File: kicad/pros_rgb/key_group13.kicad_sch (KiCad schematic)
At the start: 16 parts

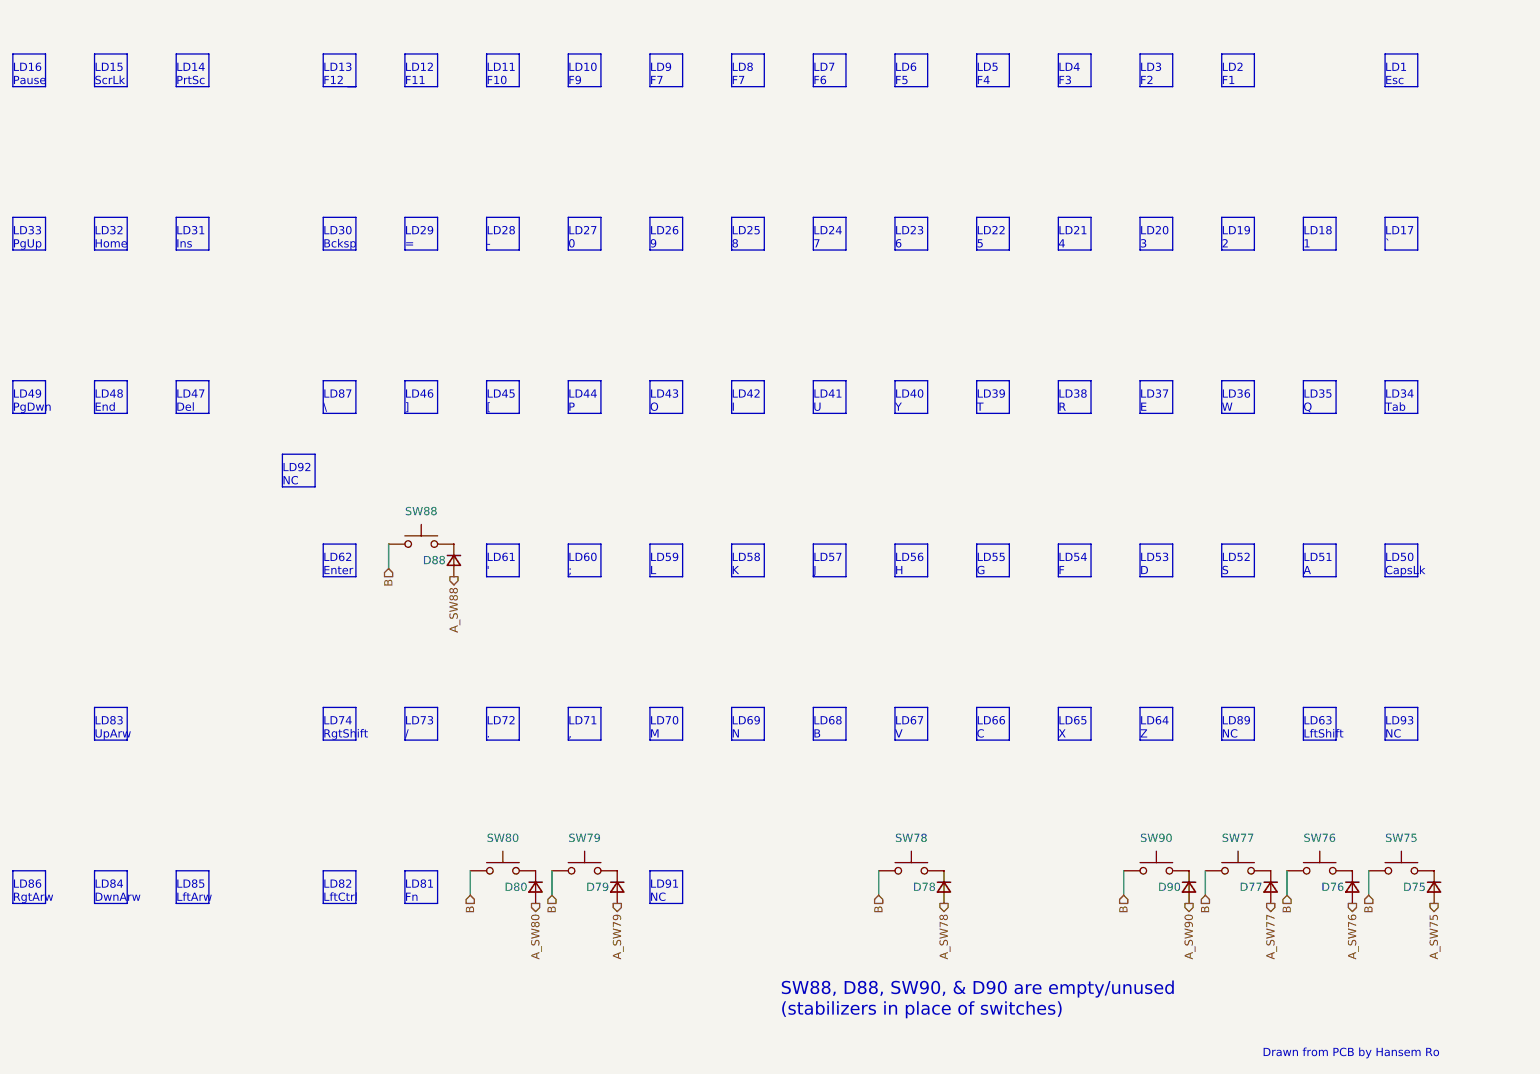
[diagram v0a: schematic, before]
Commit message: kicad/pros_rgb: update key groupings
These new groupings are based off ordering in firmware:
https://github.com/hansemro/pok3r_re_firmware/blob/4b68aa4baf7d28dc8dbf8eebcb1fdb59e7bcd629/disassemble/cmprosrgb/v122/cmprosrgb_v122.txt#L14599-L14629
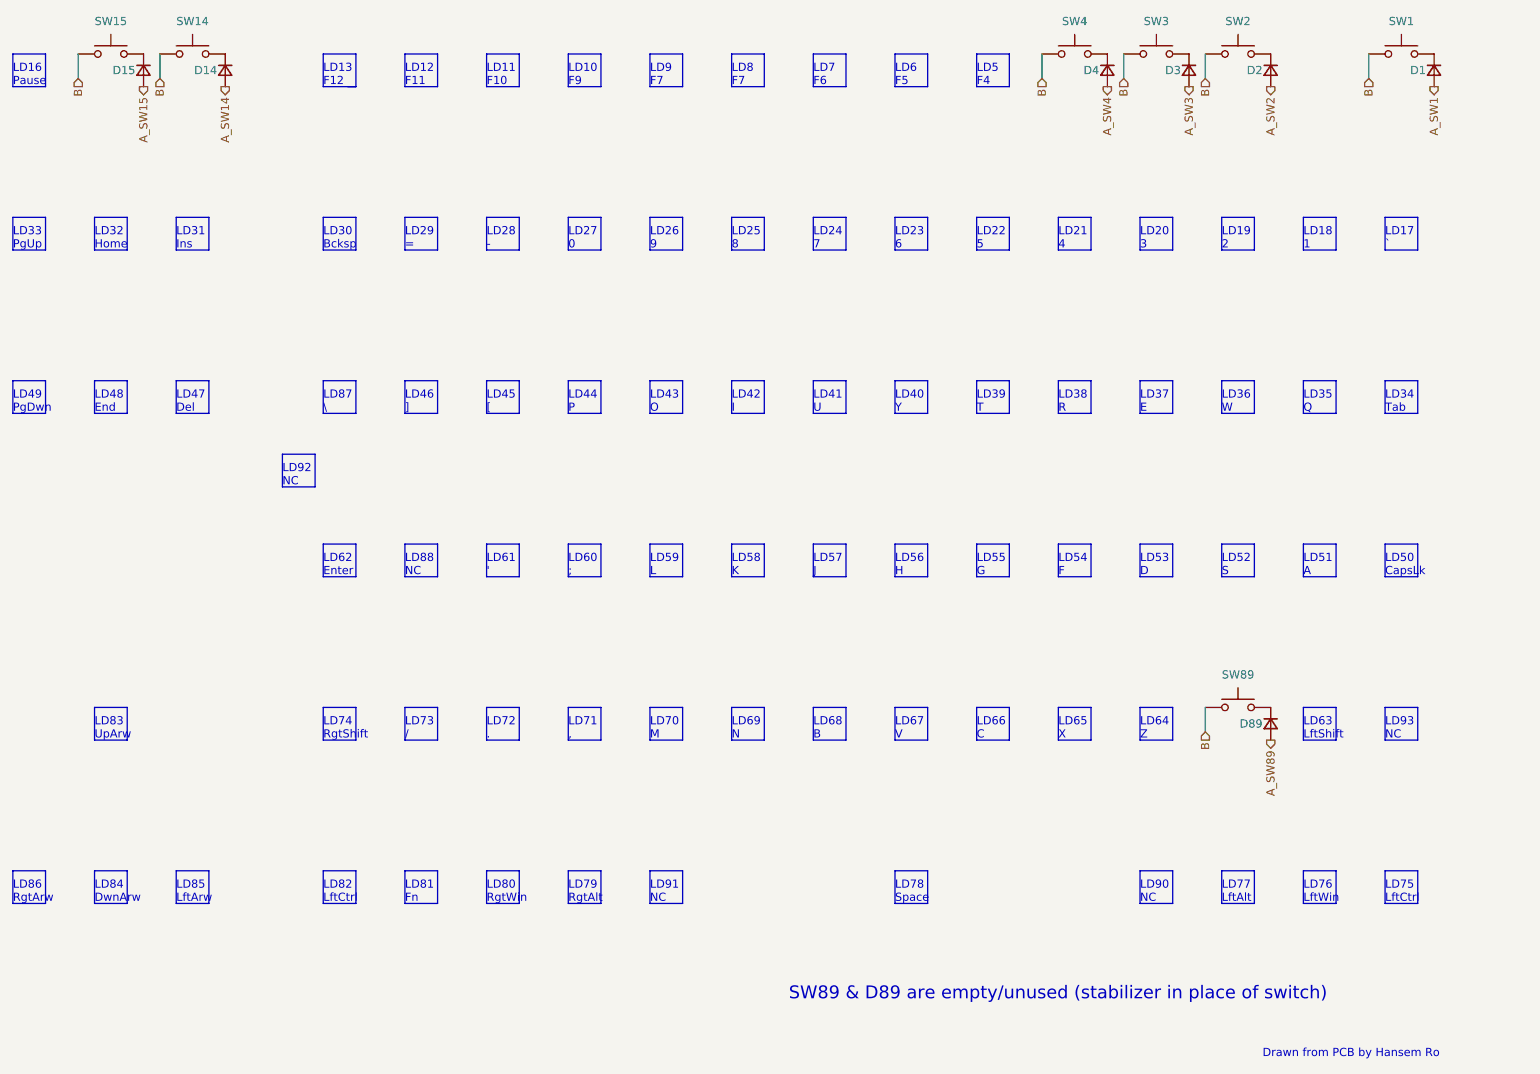
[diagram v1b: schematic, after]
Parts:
- removed D75, D76, D77, D78, D79, D80, D88, D90: ~, symbol Device:D_Small
- removed SW75, SW76, SW77, SW78, SW79, SW80, SW88, SW90: ~, symbol Switch:SW_Push
- added D1, D14, D15, D2, D3, D4, D89: (no value), symbol Device:D_Small
- added SW1, SW14, SW15, SW2, SW3, SW4, SW89: (no value), symbol Switch:SW_Push
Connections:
- net B: now also SW1.1, SW14.1, SW15.1, SW2.1, SW3.1, SW4.1, SW89.1
- new net: D3.1 (K), SW3.2
- new net: D2.1 (K), SW2.2
- new net: D15.1 (K), SW15.2
- new net: D14.1 (K), SW14.2
- new net: D1.1 (K), SW1.2
- new net: D4.1 (K), SW4.2
- new net: D89.1 (K), SW89.2
- new net A_SW1: D1.2 (A)
- new net A_SW14: D14.2 (A)
- new net A_SW15: D15.2 (A)
- new net A_SW2: D2.2 (A)
- new net A_SW3: D3.2 (A)
- new net A_SW4: D4.2 (A)
- new net A_SW89: D89.2 (A)
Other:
- note added: "LD75 LftCtrl"
- note added: "LD76 LftWin"
- note added: "LD77 LftAlt"
- note added: "LD78 Space"
- note added: "LD79 RgtAlt"
- note added: "LD80 RgtWin"
- note added: "LD88 NC"
- note added: "LD90 NC"
- note added: "SW89 & D89 are empty/unused (stabilizer in place of switch)"
- note removed: "LD1 Esc"
- note removed: "LD14 PrtSc"
- note removed: "LD15 ScrLk"
- note removed: "LD2 F1"
- note removed: "LD3 F2"
- note removed: "LD4 F3"
- note removed: "LD89 NC"
- note removed: "SW88, D88, SW90, & D90 are empty/unused (stabilizers in place of switches)"

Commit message: kicad/pros_rgb: mark as Rev. B
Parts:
- D1, D14, D15, D2, D3, D4, D89, SW1, SW14, SW15, SW2, SW3, SW4, SW89: value (none) -> ~
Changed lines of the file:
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@@
     (in_bom yes) (on_board yes)
     (property "Reference" "SW3" (id 0) (at 236.22 19.05 0))
-    (property "Value" "" (id 1) (at 236.22 19.05 0))
+    (property "Value" "~" (id 1) (at 236.22 19.05 0))
     (property "Footprint" "" (id 2) (at 236.22 19.05 0)
       (effects (font (size 1.27 1.27)) hide)
@@
       (effects (font (size 1.27 1.27)) (justify right))
     )
-    (property "Value" "" (id 1) (at 243.84 27.9399 90)
+    (property "Value" "~" (id 1) (at 243.84 27.9399 90)
       (effects (font (size 1.27 1.27)) (justify left))
     )
@@
     (in_bom yes) (on_board yes)
     (property "Reference" "SW2" (id 0) (at 248.92 19.05 0))
-    (property "Value" "" (id 1) (at 248.92 19.05 0))
+    (property "Value" "~" (id 1) (at 248.92 19.05 0))
     (property "Footprint" "" (id 2) (at 248.92 19.05 0)
       (effects (font (size 1.27 1.27)) hide)
@@
       (effects (font (size 1.27 1.27)) (justify right))
     )
-    (property "Value" "" (id 1) (at 256.54 27.9399 90)
+    (property "Value" "~" (id 1) (at 256.54 27.9399 90)
       (effects (font (size 1.27 1.27)) (justify left))
     )
@@
       (effects (font (size 1.27 1.27)) (justify right))
     )
-    (property "Value" "" (id 1) (at 81.28 27.9399 90)
+    (property "Value" "~" (id 1) (at 81.28 27.9399 90)
       (effects (font (size 1.27 1.27)) (justify left))
     )
@@
     (in_bom yes) (on_board yes)
     (property "Reference" "SW14" (id 0) (at 86.36 19.05 0))
-    (property "Value" "" (id 1) (at 86.36 19.05 0))
+    (property "Value" "~" (id 1) (at 86.36 19.05 0))
     (property "Footprint" "" (id 2) (at 86.36 19.05 0)
       (effects (font (size 1.27 1.27)) hide)
@@
       (effects (font (size 1.27 1.27)) (justify right))
     )
-    (property "Value" "" (id 1) (at 281.94 27.9399 90)
+    (property "Value" "~" (id 1) (at 281.94 27.9399 90)
       (effects (font (size 1.27 1.27)) (justify left))
     )
@@
     (in_bom yes) (on_board yes)
     (property "Reference" "SW4" (id 0) (at 223.52 19.05 0))
-    (property "Value" "" (id 1) (at 223.52 19.05 0))
+    (property "Value" "~" (id 1) (at 223.52 19.05 0))
     (property "Footprint" "" (id 2) (at 223.52 19.05 0)
       (effects (font (size 1.27 1.27)) hide)
@@
     (in_bom yes) (on_board yes)
     (property "Reference" "SW89" (id 0) (at 248.92 120.65 0))
-    (property "Value" "" (id 1) (at 248.92 120.65 0))
+    (property "Value" "~" (id 1) (at 248.92 120.65 0))
     (property "Footprint" "" (id 2) (at 248.92 120.65 0)
       (effects (font (size 1.27 1.27)) hide)
@@
     (in_bom yes) (on_board yes)
     (property "Reference" "SW15" (id 0) (at 73.66 19.05 0))
-    (property "Value" "" (id 1) (at 73.66 19.05 0))
+    (property "Value" "~" (id 1) (at 73.66 19.05 0))
     (property "Footprint" "" (id 2) (at 73.66 19.05 0)
       (effects (font (size 1.27 1.27)) hide)
@@
     (in_bom yes) (on_board yes)
     (property "Reference" "SW1" (id 0) (at 274.32 19.05 0))
-    (property "Value" "" (id 1) (at 274.32 19.05 0))
+    (property "Value" "~" (id 1) (at 274.32 19.05 0))
     (property "Footprint" "" (id 2) (at 274.32 19.05 0)
       (effects (font (size 1.27 1.27)) hide)
@@
       (effects (font (size 1.27 1.27)) (justify right))
     )
-    (property "Value" "" (id 1) (at 231.14 27.9399 90)
+    (property "Value" "~" (id 1) (at 231.14 27.9399 90)
       (effects (font (size 1.27 1.27)) (justify left))
     )
@@
       (effects (font (size 1.27 1.27)) (justify right))
     )
-    (property "Value" "" (id 1) (at 93.98 27.9399 90)
+    (property "Value" "~" (id 1) (at 93.98 27.9399 90)
       (effects (font (size 1.27 1.27)) (justify left))
     )
@@
       (effects (font (size 1.27 1.27)) (justify right))
     )
-    (property "Value" "" (id 1) (at 256.54 129.5399 90)
-      (effects (font (size 1.27 1.27)) (justify left))
-    )
+    (property "Value" "~" (id 1) (at 256.54 129.5399 90)
+      (effects (font (size 1.27 1.27)) (justify left))
+    )

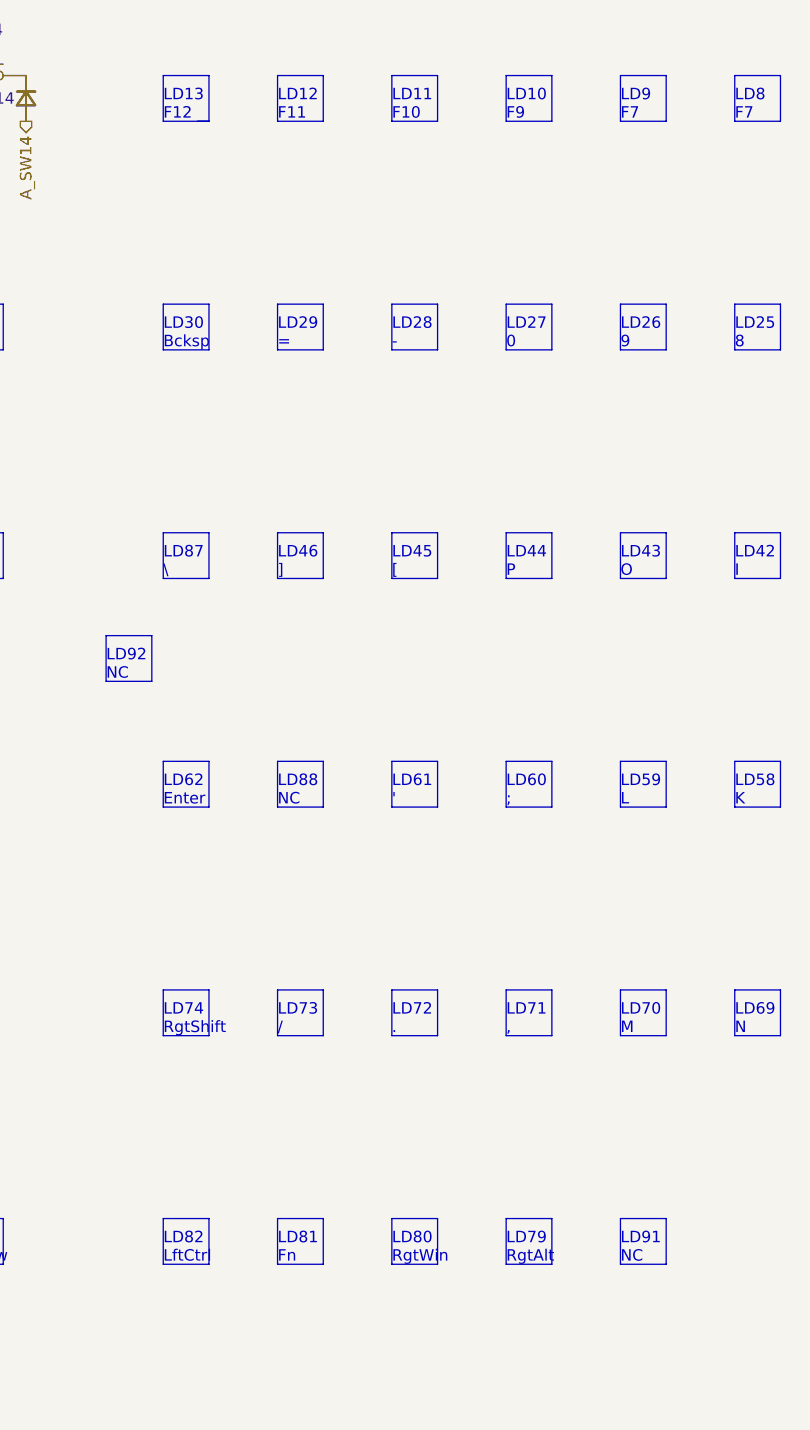
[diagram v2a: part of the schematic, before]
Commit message: kicad/pros_rgb: fix typos
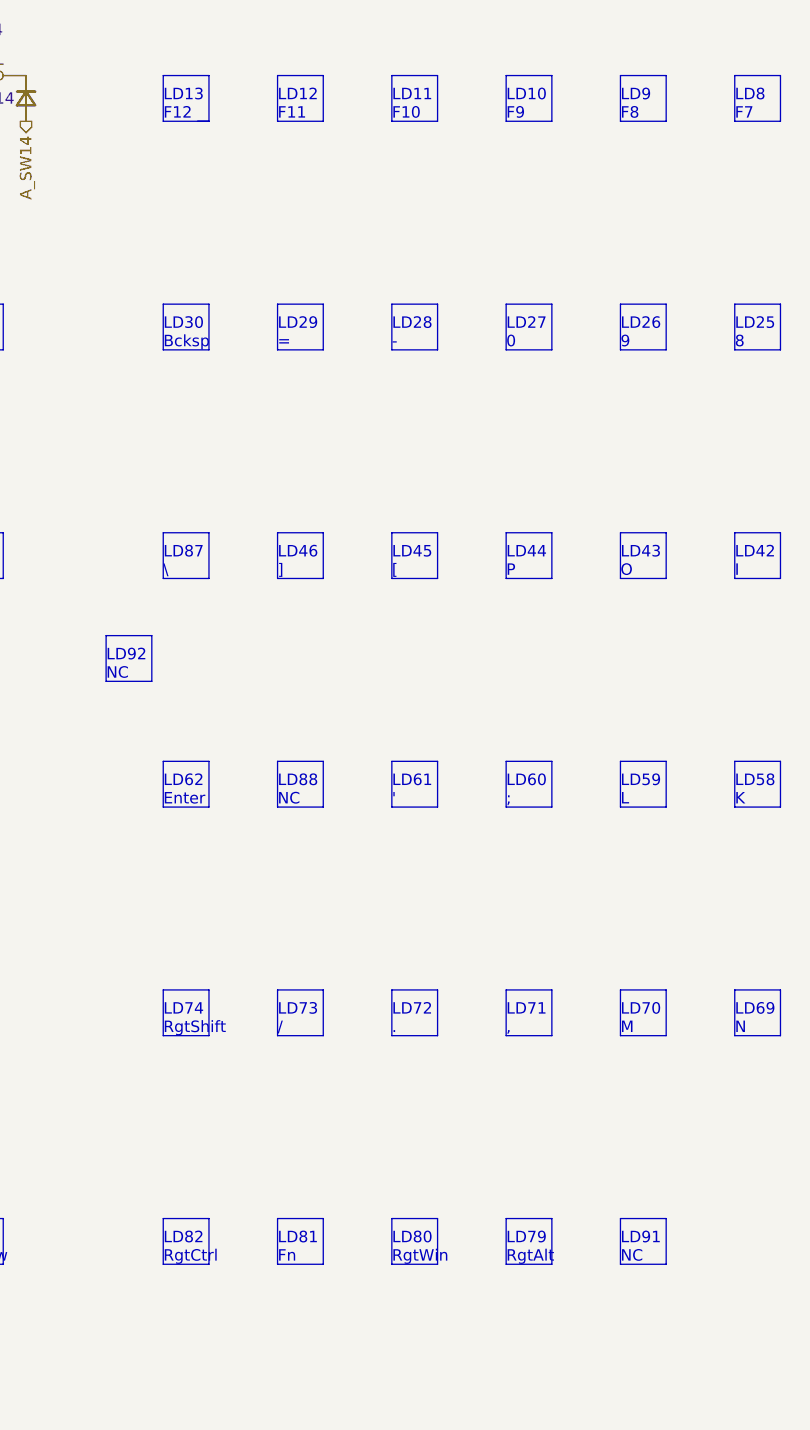
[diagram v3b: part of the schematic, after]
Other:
- note added: "LD82 RgtCtrl"
- note added: "LD9 F8"
- note removed: "LD82 LftCtrl"
- note removed: "LD9 F7"
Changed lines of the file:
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@@
     (effects (font (size 1.27 1.27)) (justify left bottom))
   )
-  (text "LD9\nF7" (at 157.48 29.21 0)
+  (text "LD9\nF8" (at 157.48 29.21 0)
     (effects (font (size 1.27 1.27)) (justify left bottom))
   )
@@
     (effects (font (size 1.27 1.27)) (justify left bottom))
   )
-  (text "LD82\nLftCtrl" (at 106.68 156.21 0)
+  (text "LD82\nRgtCtrl" (at 106.68 156.21 0)
     (effects (font (size 1.27 1.27)) (justify left bottom))
   )
